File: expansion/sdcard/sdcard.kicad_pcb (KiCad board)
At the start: 2 copper layers, 26 parts, among them J1 Conn_01x08, J2 Conn_01x10, J3 SD_Card, Q1 2N7002, Q2 2N7002, Q3 2N7002, Q4 2N7002, Q5 2N7002, Q6 2N7002, U1 74HC574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

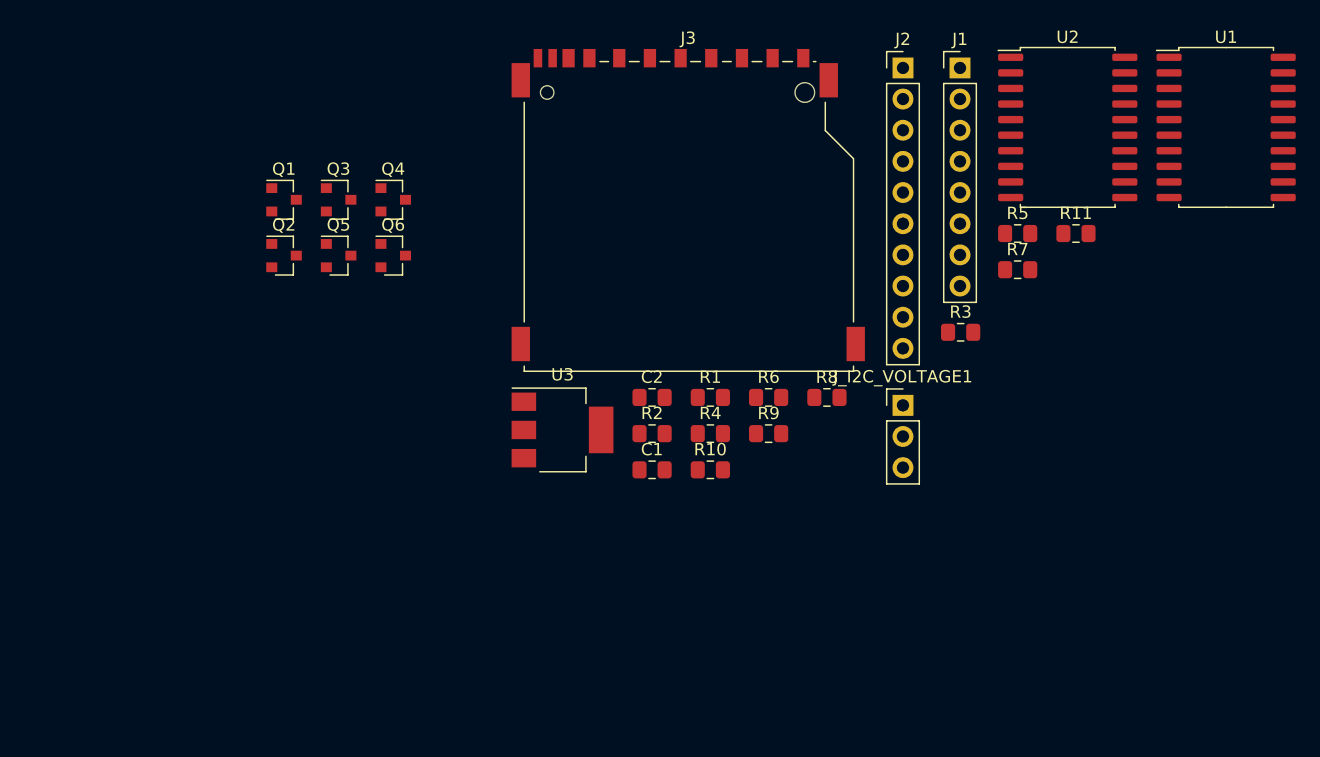
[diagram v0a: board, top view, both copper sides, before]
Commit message: SDCard expansion updated.
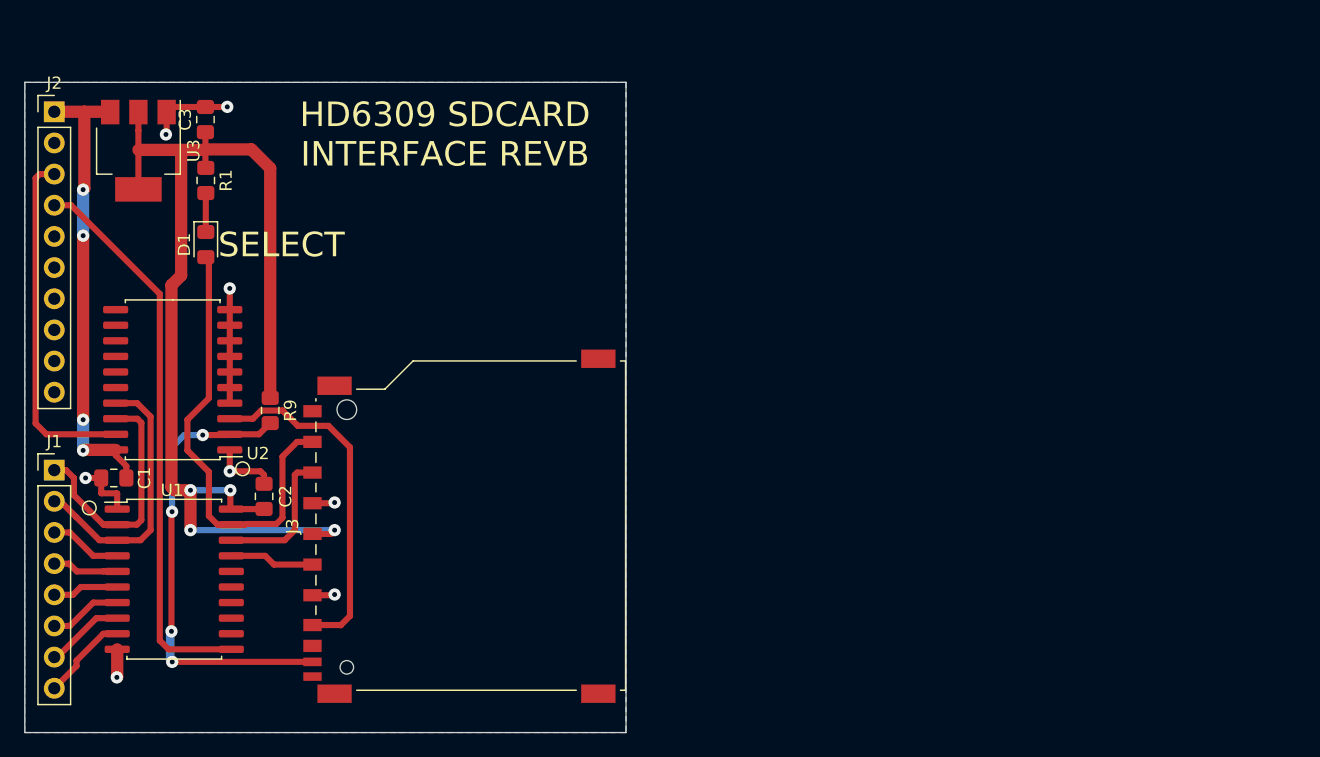
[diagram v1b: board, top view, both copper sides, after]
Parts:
- removed J_I2C_VOLTAGE1: Conn_01x03, Connector_PinHeader_2.54mm:PinHeader_1x03_P2.54mm_Vertical
- removed Q1, Q2, Q3, Q4, Q5, Q6: 2N7002, Package_TO_SOT_SMD:SOT-23
- removed R10, R11, R3, R4, R5, R6, R7, R8: 10k, Resistor_SMD:R_0805_2012Metric_Pad1.15x1.40mm_HandSolder
- removed R2: 2k2, Resistor_SMD:R_0805_2012Metric_Pad1.15x1.40mm_HandSolder
- added C3: 100n, Capacitor_SMD:C_0805_2012Metric_Pad1.15x1.40mm_HandSolder, F.Cu at (37.7, 26.0)
- added D1: LED_Small, LED_SMD:LED_0805_2012Metric_Pad1.15x1.40mm_HandSolder, F.Cu at (37.8, 36.2)
- R1: value 2k2 -> 470
- U1: value 74HC574 -> 74LVX574
- moved U1 93.3 mm to (35.2, 63.5)
- moved J1 80.8 mm to (25.4, 54.6)
- moved U2 75.8 mm to (35.1, 47.2), turned to 180 degrees
- moved J2 69.3 mm to (25.4, 25.4)
- moved R1 44.8 mm to (37.8, 31.0), turned to 270 degrees
- moved C1 43.9 mm to (30.2, 55.2), turned to 180 degrees
- moved U3 41.4 mm to (32.3, 28.6), turned to 270 degrees
- moved R9 40.7 mm to (43.0, 49.8), turned to 270 degrees
- moved C2 32.6 mm to (42.5, 56.8), turned to 90 degrees
- moved J3 32.1 mm to (58.4, 59.2), turned to 90 degrees
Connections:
- net GPIO0 renamed Net-(U1-Pad16)
- net GPIO1 renamed Net-(U1-Pad15)
- net GPIO2 renamed Net-(U1-Pad14)
- J3 pad 7: MISO_3V -> MISO
- R1 pad 1: Net-(J_I2C_VOLTAGE1-Pad2) -> +3V3
- R1 pad 2: I2C_SCL -> Net-(D1-Pad1)
- U1 pad 12: SCL -> Net-(U1-Pad12)
- U1 pad 13: SDA -> Net-(U1-Pad13)
- U1 pad 17: ~SS -> SCK_3V
- U1 pad 18: SCK -> MOSI_3V
- U1 pad 19: MOSI -> ~SS_3V
- U1 pad 20: +5V -> +3V3
- U2 pad 11: Net-(J1-Pad1) -> Net-(U2-Pad11)
- U2 pad 12: Net-(J1-Pad2) -> Net-(U2-Pad12)
- U2 pad 17: Net-(U2-Pad17) -> Net-(J1-Pad2)
- U2 pad 18: Net-(J1-Pad8) -> Net-(J1-Pad1)
- U2 pad 2: MISO -> CARD_DETECT
- U2 pad 3: CARD_DETECT -> MISO
- U2 pad 4: Net-(U2-Pad4) -> GND
- U2 pad 5: Net-(U2-Pad5) -> GND
- U2 pad 6: Net-(U2-Pad6) -> GND
- U2 pad 7: Net-(U2-Pad7) -> GND
- U2 pad 8: Net-(U2-Pad8) -> GND
- U2 pad 9: I2C_SDA -> GND
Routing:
- net +3V3: track 0.00 -> 93.2 mm, vias 0 -> 4
- net ~WR: track 0.00 -> 46.0 mm
- net CARD_DETECT: track 0.00 -> 40.6 mm, vias 0 -> 4
- net +5V: track 0.00 -> 37.5 mm, vias 0 -> 4
- net ~SS_3V: track 0.00 -> 37.1 mm
- net GND: track 0.00 -> 32.9 mm, vias 0 -> 8
- net ~RD: track 0.00 -> 28.5 mm
- net MISO: track 0.00 -> 28.4 mm
- net Net-(J1-Pad2): track 0.00 -> 22.1 mm
- net Net-(J1-Pad1): track 0.00 -> 20.1 mm
- net MOSI_3V: track 0.00 -> 11.5 mm
- net Net-(J1-Pad8): track 0.00 -> 7.23 mm
- net SCK_3V: track 0.00 -> 6.91 mm
- net Net-(J1-Pad7): track 0.00 -> 6.44 mm
- net Net-(J1-Pad6): track 0.00 -> 5.92 mm
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- added copper zone on B.Cu, net GND
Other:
- board outline added: 49 x 53 mm
- board text added: "HD6309 SDCARD INTERFACE REVB"
- board text added: "SELECT"
